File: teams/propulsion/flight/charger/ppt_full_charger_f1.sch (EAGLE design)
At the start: 95 parts, among them Q1 MOSFET-NCHANNELFDD8780, Q2 MOSFET-NCHANNELFDD8780, U1 LT3750EMS, U2 LT3750EMS, U4 MICREL_MOSFETDRIVER_MIC4420

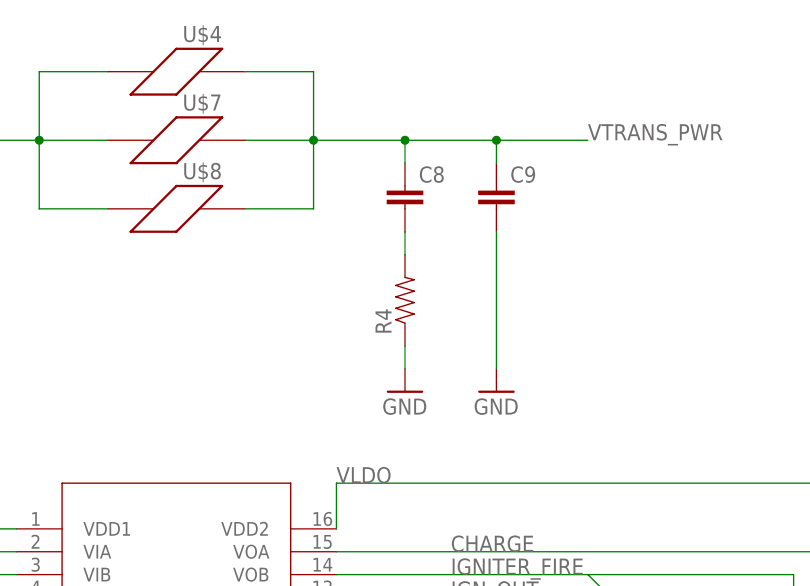
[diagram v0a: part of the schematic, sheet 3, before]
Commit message: moved power connector due to collision with aluminum on below board
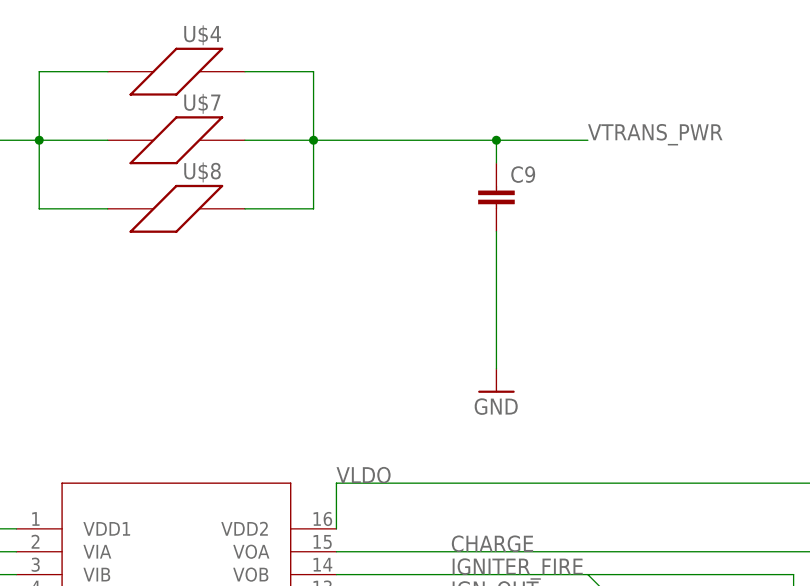
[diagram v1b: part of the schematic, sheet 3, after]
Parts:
- removed C8: (no value), SparkFun-Capacitors:CAP0805
- removed R4: (no value), SparkFun-Passives:RESISTOR0805-RES
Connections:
- removed net N$28: C8.2, R4.2
- net GND: no longer R4.1
- net VTRANS_PWR: no longer C8.1
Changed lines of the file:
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@@
 <?xml version="1.0" encoding="utf-8"?>
 <!DOCTYPE eagle SYSTEM "eagle.dtd">
-<eagle version="7.5.0">
+<eagle version="8.7.1">
 <drawing>
 <settings>
 <setting alwaysvectorfont="no"/>
+<setting keepoldvectorfont="yes"/>
 <setting verticaltext="up"/>
 </settings>
@@
 <part name="U$7" library="Ferrite" deviceset="B.L2_FBMH1608HL121-T" device=""/>
 <part name="U$8" library="Ferrite" deviceset="I.L1_587-3855-1-ND" device=""/>
-<part name="R4" library="SparkFun-Passives" deviceset="RESISTOR" device="0805-RES"/>
 <part name="GND30" library="SparkFun-Aesthetics" deviceset="GND" device=""/>
-<part name="GND31" library="SparkFun-Aesthetics" deviceset="GND" device=""/>
 <part name="GND32" library="SparkFun-Aesthetics" deviceset="GND" device=""/>
 <part name="C7" library="SparkFun-Capacitors" deviceset="CAP" device="0805"/>
-<part name="C8" library="SparkFun-Capacitors" deviceset="CAP" device="0805"/>
 <part name="C9" library="SparkFun-Capacitors" deviceset="CAP" device="0805"/>
 <part name="J1" library="SparkFun-Connectors" deviceset="M08" device=""/>
@@
 <instance part="U$7" gate="B.L2" x="68.58" y="73.66"/>
 <instance part="U$8" gate="I.L1" x="68.58" y="66.04"/>
-<instance part="R4" gate="G$1" x="93.98" y="55.88" rot="R90"/>
 <instance part="GND30" gate="1" x="104.14" y="45.72"/>
-<instance part="GND31" gate="1" x="93.98" y="45.72"/>
 <instance part="GND32" gate="1" x="43.18" y="48.26"/>
 <instance part="C7" gate="G$1" x="43.18" y="66.04"/>
-<instance part="C8" gate="G$1" x="93.98" y="66.04"/>
 <instance part="C9" gate="G$1" x="104.14" y="66.04"/>
 <instance part="ADUM163N" gate="A" x="48.26" y="30.48"/>
@@
 </segment>
 <segment>
-<pinref part="R4" gate="G$1" pin="1"/>
-<pinref part="GND31" gate="1" pin="GND"/>
-<wire x1="93.98" y1="50.8" x2="93.98" y2="48.26" width="0.1524" layer="91"/>
-</segment>
-<segment>
 <pinref part="GND32" gate="1" pin="GND"/>
 <wire x1="43.18" y1="50.8" x2="43.18" y2="63.5" width="0.1524" layer="91"/>
@@
 <wire x1="76.2" y1="73.66" x2="83.82" y2="73.66" width="0.1524" layer="91"/>
 <junction x="83.82" y="73.66"/>
-<wire x1="83.82" y1="73.66" x2="93.98" y2="73.66" width="0.1524" layer="91"/>
-<wire x1="93.98" y1="73.66" x2="104.14" y2="73.66" width="0.1524" layer="91"/>
+<wire x1="83.82" y1="73.66" x2="104.14" y2="73.66" width="0.1524" layer="91"/>
 <wire x1="104.14" y1="73.66" x2="104.14" y2="71.12" width="0.1524" layer="91"/>
-<wire x1="93.98" y1="71.12" x2="93.98" y2="73.66" width="0.1524" layer="91"/>
-<junction x="93.98" y="73.66"/>
 <wire x1="104.14" y1="73.66" x2="114.3" y2="73.66" width="0.1524" layer="91"/>
 <junction x="104.14" y="73.66"/>
 <label x="114.3" y="73.66" size="1.778" layer="95"/>
-<pinref part="C8" gate="G$1" pin="1"/>
 <pinref part="C9" gate="G$1" pin="1"/>
 </segment>
@@
 </segment>
 </net>
-<net name="N$28" class="0">
-<segment>
-<pinref part="R4" gate="G$1" pin="2"/>
-<wire x1="93.98" y1="60.96" x2="93.98" y2="63.5" width="0.1524" layer="91"/>
-<pinref part="C8" gate="G$1" pin="2"/>
-</segment>
-</net>
